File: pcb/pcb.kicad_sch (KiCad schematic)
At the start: 34 parts, among them J1 Conn_01x20_Socket, J10 Conn_01x01_Socket, J11 Conn_01x01_Socket, J12 Conn_01x01_Socket, J13 Conn_01x01_Socket, J14 Conn_01x01_Socket, J15 Conn_01x01_Socket, J16 Conn_01x01_Socket, J17 Conn_01x01_Socket, J18 Conn_01x01_Socket, J19 Conn_01x01_Socket, J2 Conn_01x20_Socket, J20 Conn_01x01_Socket, J21 Conn_01x01_Socket, J22 Conn_01x01_Socket, J23 Conn_01x01_Socket, J24 Conn_01x01_Socket, J25 Conn_01x01_Socket, J26 Conn_01x01_Socket, J27 Conn_01x01_Socket, J28 Conn_01x01_Socket, J29 Conn_01x01_Socket, J3 Conn_01x01_Socket, J30 Conn_01x01_Socket, J31 Conn_01x01_Socket, J32 Conn_01x01_Socket, J33 Conn_01x01_Socket, J34 Conn_01x01_Socket, J4 Conn_01x01_Socket, J5 Conn_01x01_Socket, J6 Conn_01x01_Socket, J7 Conn_01x01_Socket, J8 Conn_01x01_Socket, J9 Conn_01x01_Socket

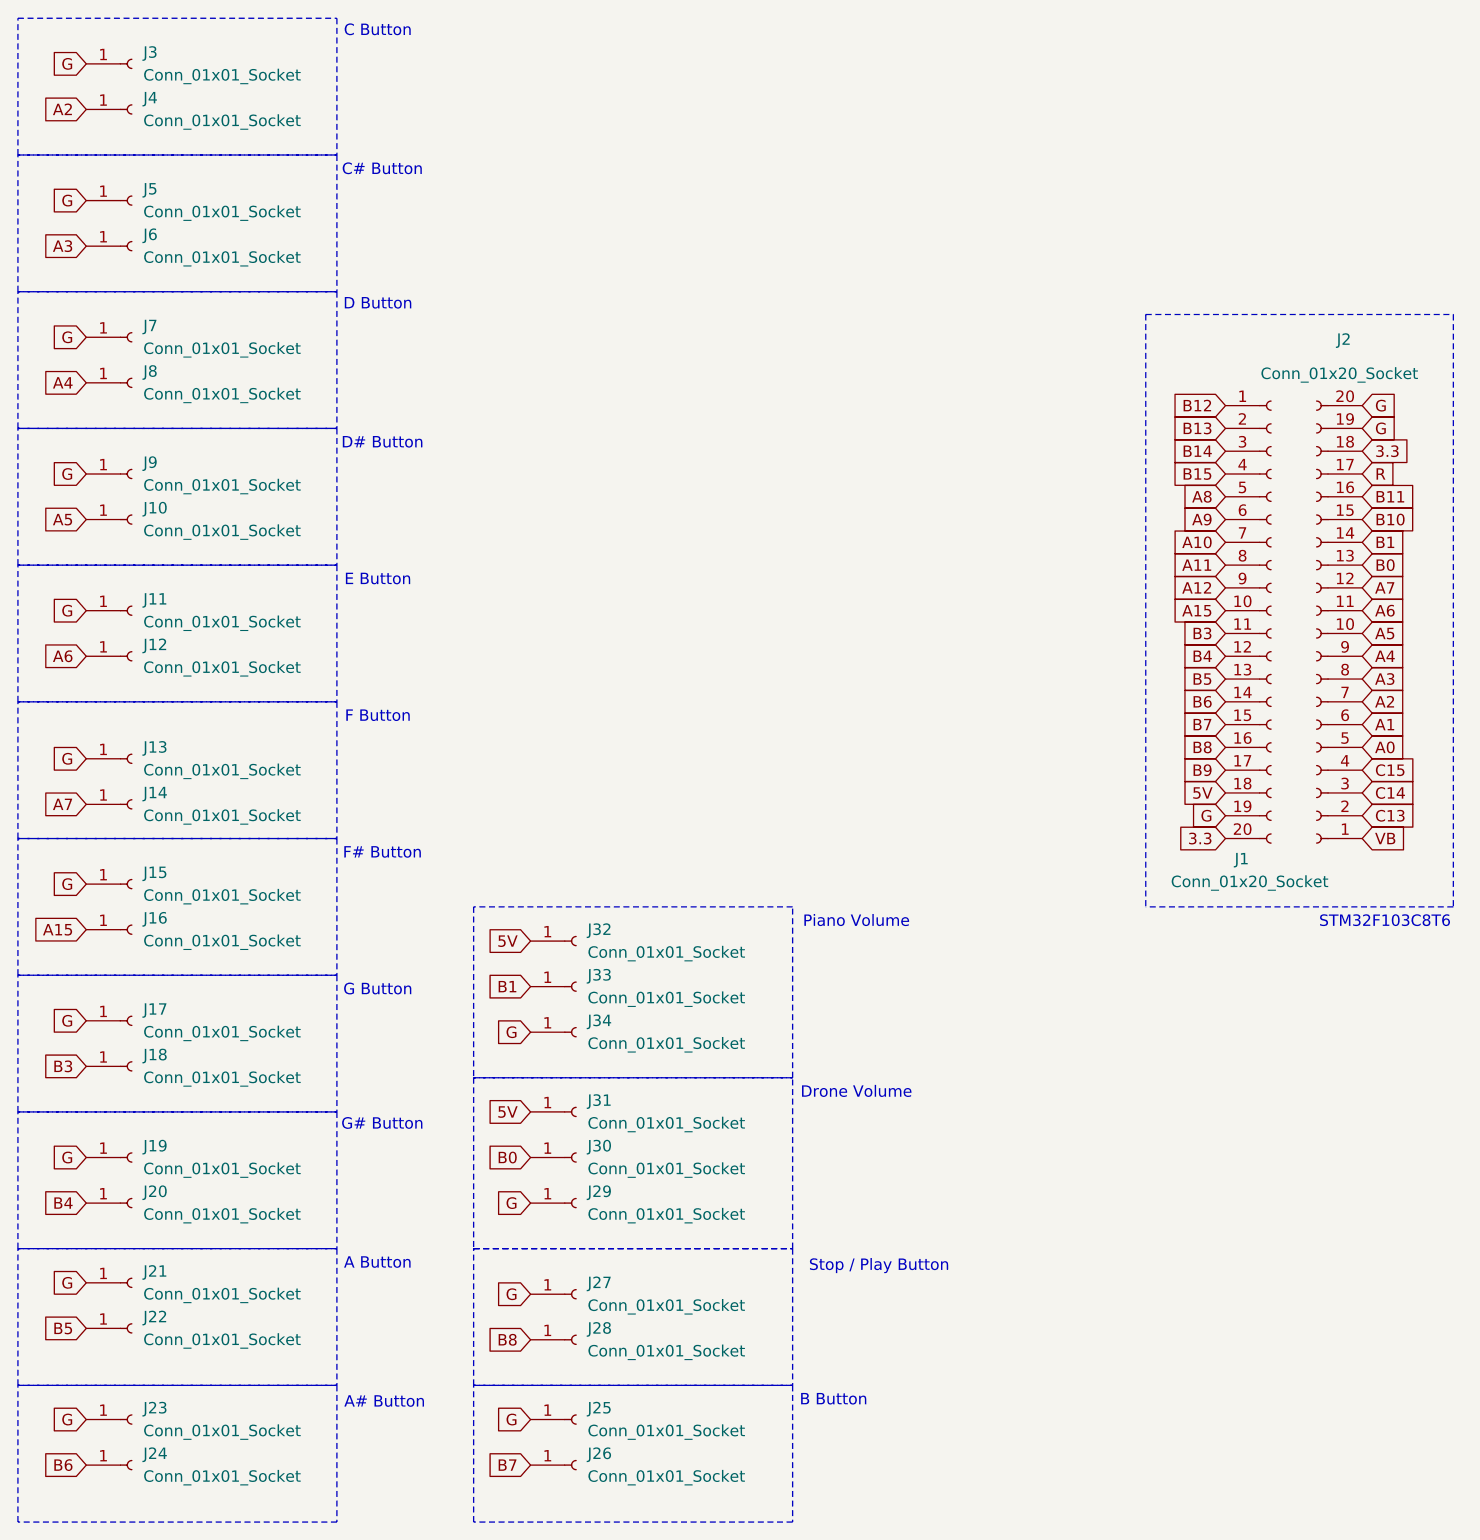
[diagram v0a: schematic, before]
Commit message: I accidentally set up the project using the wrong folder, so I hope this fixes it. All these new files are the real project. Anyway, fixed issues with ADC breaking the MIDI connection. Small crash when doing multiple inputs at the same time. Next is to finally finish the PCB.
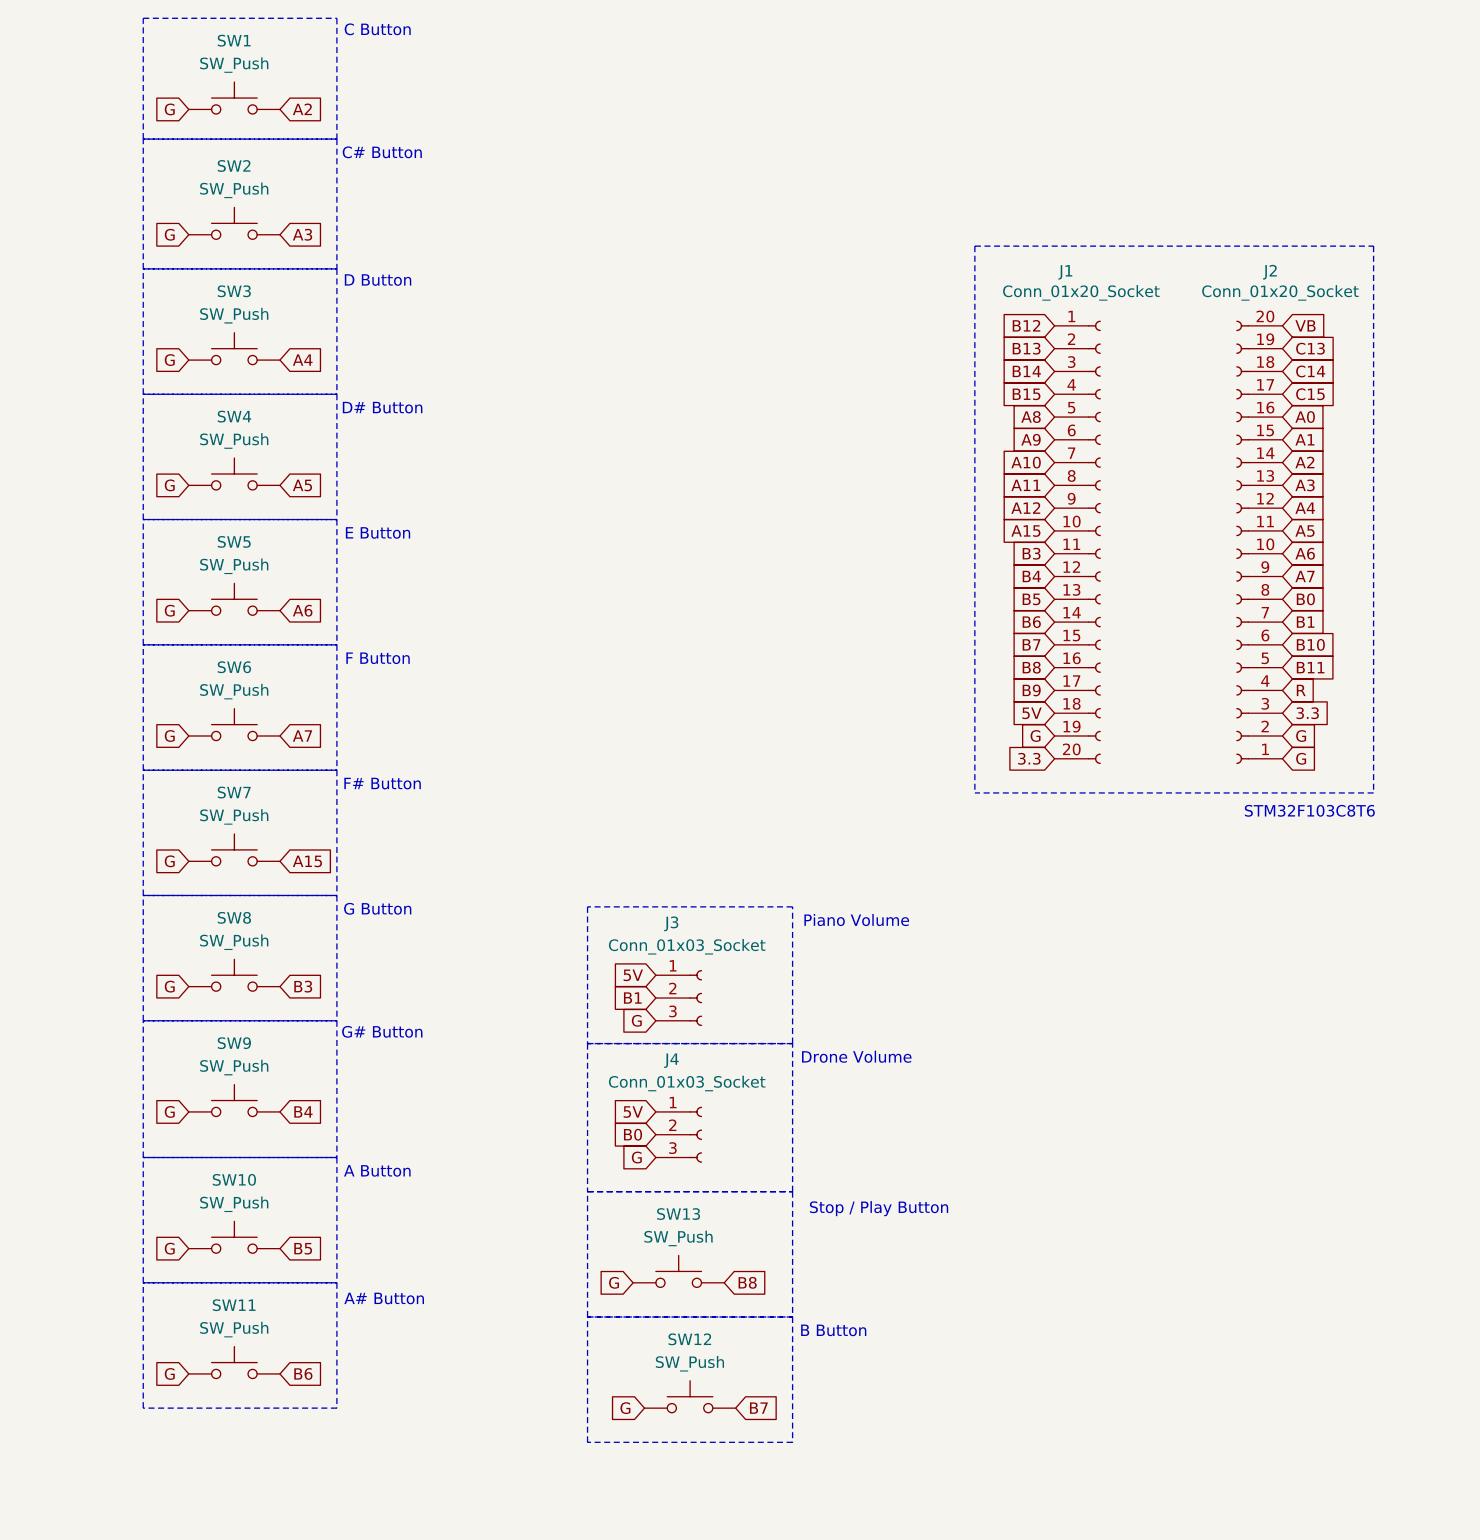
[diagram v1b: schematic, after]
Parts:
- removed J10, J11, J12, J13, J14, J15, J16, J17, J18, J19, J20, J21, J22, J23, J24, J25, J26, J27, J28, J29, J3, J30, J31, J32, J33, J34, J4, J5, J6, J7, J8, J9: Conn_01x01_Socket, Connector_Wire:SolderWire-0.5sqmm_1x01_D0.9mm_OD2.1mm, symbol Connector:Conn_01x01_Socket
- added J3, J4: Conn_01x03_Socket, Potentiometer_THT:Potentiometer_Alpha_RD901F-40-00D_Single_Vertical_CircularHoles, symbol Connector:Conn_01x03_Socket
- added SW1, SW10, SW11, SW12, SW13, SW2, SW3, SW4, SW5, SW6, SW7, SW8, SW9: SW_Push, Button_Switch_Keyboard:SW_Cherry_MX_1.00u_Plate, symbol Switch:SW_Push
- J1, J2: footprint Connector_TE-Connectivity:TE_2-826576-0_1x20_P3.96mm_Vertical -> Connector_PinHeader_2.54mm:PinHeader_1x20_P2.54mm_Vertical
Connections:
- net 3.3: now also J2.3 (Pin_3); no longer J2.18 (Pin_18)
- net 5V: now also J3.1 (Pin_1), J4.1 (Pin_1)
- net A0: now also J2.16 (Pin_16); no longer J2.5 (Pin_5)
- net A1: now also J2.15 (Pin_15); no longer J2.6 (Pin_6)
- net A15: now also SW7.2
- net A2: now also J2.14 (Pin_14), SW1.2; no longer J2.7 (Pin_7)
- net A3: now also J2.13 (Pin_13), SW2.2; no longer J2.8 (Pin_8)
- net A4: now also J2.12 (Pin_12), SW3.2; no longer J2.9 (Pin_9)
- net A5: now also J2.11 (Pin_11), SW4.2; no longer J2.10 (Pin_10)
- net A6: now also J2.10 (Pin_10), SW5.2; no longer J2.11 (Pin_11)
- net A7: now also J2.9 (Pin_9), SW6.2; no longer J2.12 (Pin_12)
- net B0: now also J2.8 (Pin_8), J4.2 (Pin_2); no longer J2.13 (Pin_13)
- net B1: now also J2.7 (Pin_7), J3.2 (Pin_2); no longer J2.14 (Pin_14)
- net B10: now also J2.6 (Pin_6); no longer J2.15 (Pin_15)
- net B11: now also J2.5 (Pin_5); no longer J2.16 (Pin_16)
- net B3: now also SW8.2
- net B4: now also SW9.2
- net B5: now also SW10.2
- net B6: now also SW11.2
- net B7: now also SW12.2
- net B8: now also SW13.2
- net C13: now also J2.19 (Pin_19); no longer J2.2 (Pin_2)
- net C14: now also J2.18 (Pin_18); no longer J2.3 (Pin_3)
- net C15: now also J2.17 (Pin_17); no longer J2.4 (Pin_4)
- net G: now also J2.1 (Pin_1), J2.2 (Pin_2), J3.3 (Pin_3), J4.3 (Pin_3), SW1.1, SW10.1, SW11.1, SW12.1, SW13.1, SW2.1, SW3.1, SW4.1, SW5.1, SW6.1, SW7.1, SW8.1, SW9.1; no longer J2.19 (Pin_19), J2.20 (Pin_20)
- net R: now also J2.4 (Pin_4); no longer J2.17 (Pin_17)
- net VB: now also J2.20 (Pin_20); no longer J2.1 (Pin_1)
